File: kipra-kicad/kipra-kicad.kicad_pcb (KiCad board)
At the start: 2 copper layers, 128.2 x 134.8 mm, 51 parts

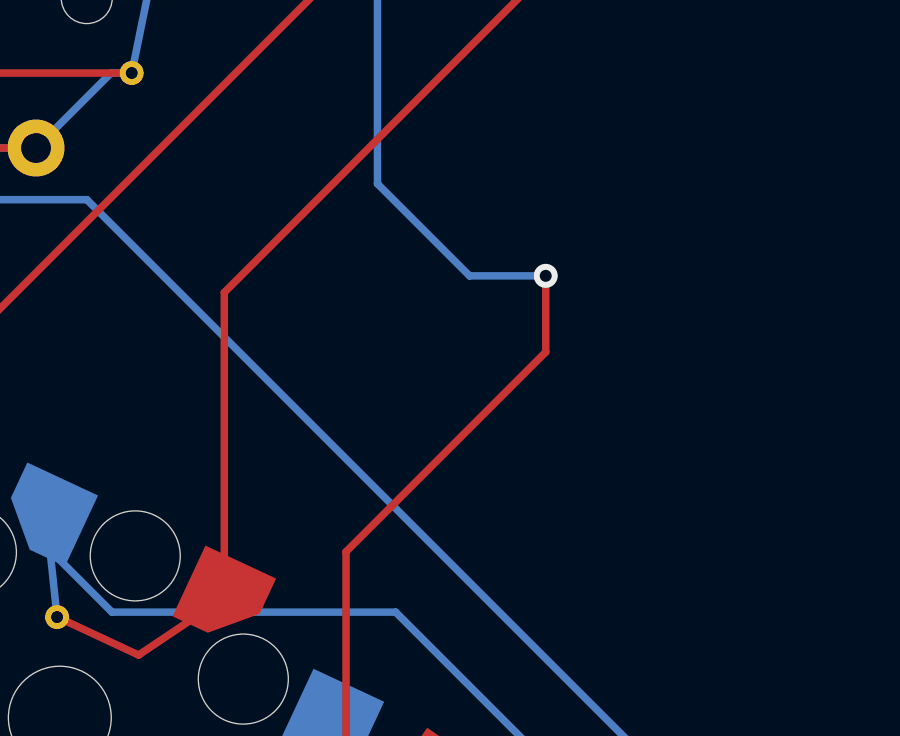
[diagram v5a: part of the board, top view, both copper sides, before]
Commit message: about to edit kicad pcb file by hand to fix row to mcu traces
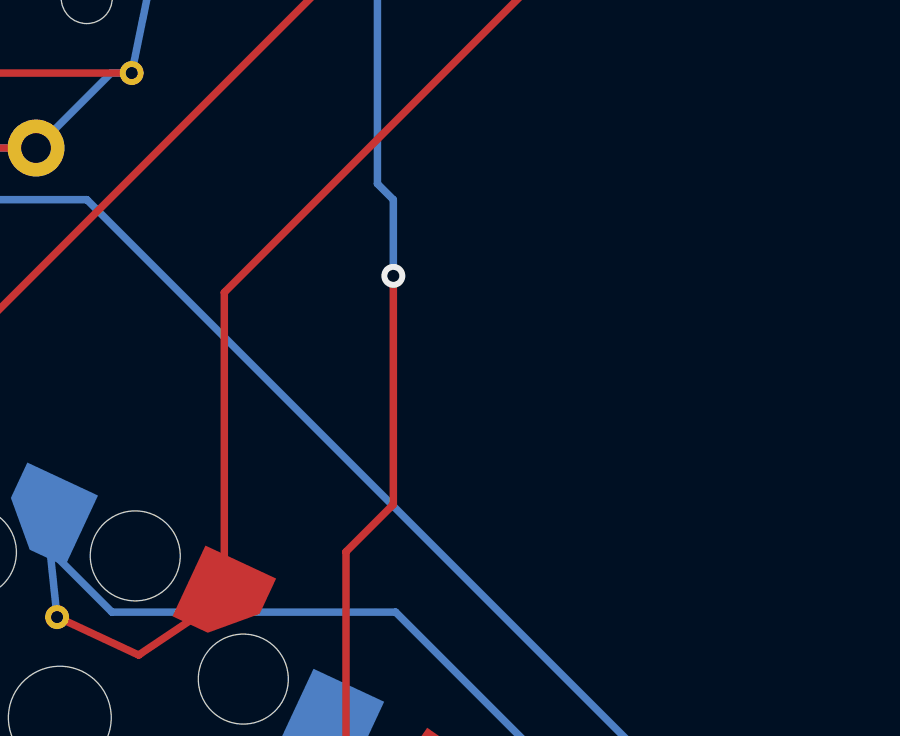
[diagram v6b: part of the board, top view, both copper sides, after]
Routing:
- net P07: track 158.1 -> 152.4 mm
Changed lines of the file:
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@@
   (segment (start 189.862146 123.877924) (end 162.504222 96.52) (width 0.25) (layer "B.Cu") (net 29))
   (segment (start 115.19 94.8) (end 117.35 94.8) (width 0.25) (layer "B.Cu") (net 29))
-  (segment (start 177.8 101.6) (end 171.142994 108.257006) (width 0.25) (layer "F.Cu") (net 30))
+  (segment (start 171.142994 123.996442) (end 172.808353 125.661801) (width 0.25) (layer "F.Cu") (net 30))
   (segment (start 172.19 80.35) (end 174.35 80.35) (width 0.25) (layer "F.Cu") (net 30))
+  (segment (start 172.72 106.68) (end 171.142994 108.257006) (width 0.25) (layer "F.Cu") (net 30))
   (segment (start 171.26 81.28) (end 172.19 80.35) (width 0.25) (layer "F.Cu") (net 30))
   (segment (start 115.19 77.8) (end 115.19 78.335305) (width 0.25) (layer "F.Cu") (net 30))
   (segment (start 98.35 88) (end 96.19 88) (width 0.25) (layer "F.Cu") (net 30))
+  (segment (start 172.72 99.06) (end 172.72 106.68) (width 0.25) (layer "F.Cu") (net 30))
   (segment (start 138.365 77.725) (end 153.115 77.725) (width 0.25) (layer "F.Cu") (net 30))
   (segment (start 119.125 76.025) (end 131.715 76.025) (width 0.25) (layer "F.Cu") (net 30))
   (segment (start 172.808353 125.661801) (end 173.338796 125.661801) (width 0.25) (layer "F.Cu") (net 30))
-  (segment (start 171.142994 123.996442) (end 172.808353 125.661801) (width 0.25) (layer "F.Cu") (net 30))
   (segment (start 158.83 81.28) (end 171.26 81.28) (width 0.25) (layer "F.Cu") (net 30))
   (segment (start 155.35 77.8) (end 158.83 81.28) (width 0.25) (layer "F.Cu") (net 30))
-  (segment (start 171.142994 108.257006) (end 171.142994 123.996442) (width 0.25) (layer "F.Cu") (net 30))
   (segment (start 131.715 76.025) (end 134.19 73.55) (width 0.25) (layer "F.Cu") (net 30))
   (segment (start 107.165305 86.36) (end 99.99 86.36) (width 0.25) (layer "F.Cu") (net 30))
   (segment (start 134.19 73.55) (end 138.365 77.725) (width 0.25) (layer "F.Cu") (net 30))
   (segment (start 99.99 86.36) (end 98.35 88) (width 0.25) (layer "F.Cu") (net 30))
+  (segment (start 171.142994 108.257006) (end 171.142994 123.996442) (width 0.25) (layer "F.Cu") (net 30))
   (segment (start 115.19 78.335305) (end 107.165305 86.36) (width 0.25) (layer "F.Cu") (net 30))
   (segment (start 117.35 77.8) (end 115.19 77.8) (width 0.25) (layer "F.Cu") (net 30))
@@
   (segment (start 153.19 77.8) (end 155.35 77.8) (width 0.25) (layer "F.Cu") (net 30))
   (segment (start 153.115 77.725) (end 153.19 77.8) (width 0.25) (layer "F.Cu") (net 30))
-  (segment (start 177.8 99.06) (end 177.8 101.6) (width 0.25) (layer "F.Cu") (net 30))
-  (via (at 177.8 99.06) (size 0.8) (drill 0.4) (layers "F.Cu" "B.Cu") (net 30))
+  (via (at 172.72 99.06) (size 0.8) (drill 0.4) (layers "F.Cu" "B.Cu") (net 30))
+  (segment (start 172.72 96.52) (end 172.19 95.99) (width 0.25) (layer "B.Cu") (net 30))
   (segment (start 172.808353 125.661801) (end 173.338796 125.661801) (width 0.25) (layer "B.Cu") (net 30))
-  (segment (start 177.8 99.06) (end 175.26 99.06) (width 0.25) (layer "B.Cu") (net 30))
+  (segment (start 172.72 99.06) (end 172.72 96.52) (width 0.25) (layer "B.Cu") (net 30))
   (segment (start 172.19 80.35) (end 174.35 80.35) (width 0.25) (layer "B.Cu") (net 30))
   (segment (start 153.19 77.8) (end 155.35 77.8) (width 0.25) (layer "B.Cu") (net 30))
   (segment (start 173.338796 125.661801) (end 174.577721 126.900726) (width 0.25) (layer "B.Cu") (net 30))
+  (segment (start 172.19 95.99) (end 172.19 80.35) (width 0.25) (layer "B.Cu") (net 30))
   (segment (start 134.19 73.55) (end 136.35 73.55) (width 0.25) (layer "B.Cu") (net 30))
   (segment (start 115.19 77.8) (end 117.35 77.8) (width 0.25) (layer "B.Cu") (net 30))
-  (segment (start 172.19 95.99) (end 172.19 80.35) (width 0.25) (layer "B.Cu") (net 30))
-  (segment (start 175.26 99.06) (end 172.19 95.99) (width 0.25) (layer "B.Cu") (net 30))
   (segment (start 98.35 88) (end 96.19 88) (width 0.25) (layer "B.Cu") (net 30))
   (segment (start 107.3 69.225) (end 115.19 61.335) (width 0.25) (layer "F.Cu") (net 31))

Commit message: hand editing pcb file seems to have fixed the row to mcu traces
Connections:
- D1 pad 1: P08 -> P8
- D10 pad 1: P07 -> P7
- D11 pad 1: P06 -> P6
- D12 pad 1: P05 -> P5
- D13 pad 1: P08 -> P8
- D14 pad 1: P07 -> P7
- D15 pad 1: P06 -> P6
- D16 pad 1: P05 -> P5
- D17 pad 1: P07 -> P7
- D18 pad 1: P06 -> P6
- D19 pad 1: P05 -> P5
- D2 pad 1: P07 -> P7
- D20 pad 1: P08 -> P8
- D21 pad 1: P07 -> P7
- D22 pad 1: P06 -> P6
- D3 pad 1: P06 -> P6
- D4 pad 1: P05 -> P5
- D5 pad 1: P08 -> P8
- D6 pad 1: P07 -> P7
- D7 pad 1: P06 -> P6
- D8 pad 1: P05 -> P5
- D9 pad 1: P08 -> P8
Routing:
- net P6: track 10.2 -> 183.6 mm
- net P06: track 173.4 -> 0.00 mm
- net P7: track 10.2 -> 162.6 mm, vias 0 -> 1
- net P07: track 152.4 -> 0.00 mm, vias 1 -> 0
- net P8: track 10.2 -> 151.7 mm
- net P08: track 141.6 -> 0.00 mm
- net P05: track 98.1 -> 0.00 mm
- net P5: track 10.2 -> 108.2 mm

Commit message: DRC passes!
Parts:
- MCU1: footprint nice_nano -> ceoloide:nice_nano
- moved _3 15.5 mm to (201.1, 84.8)
- moved D16 2.71 mm to (156.1, 41.2)
- moved MCU1 2.71 mm to (197.1, 43.8)
- moved D11 2.71 mm to (137.1, 54.0)
- moved D15 2.71 mm to (156.1, 58.2)
- moved D2 2.71 mm to (99.1, 85.4)
- moved S17 2.71 mm to (175.1, 72.8)
- moved S6 2.71 mm to (118.1, 70.2)
- moved S3 2.71 mm to (99.1, 63.4)
- moved S4 2.71 mm to (99.1, 46.4)
- moved D7 2.71 mm to (118.1, 58.2)
- moved S16 2.71 mm to (156.1, 36.2)
- moved _1 2.71 mm to (99.1, 110.2)
- moved S12 2.71 mm to (137.1, 32.0)
- moved _2 2.71 mm to (99.1, 33.7)
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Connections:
- MCU1 pad 13: MCU1_13 -> MCU1_12
- MCU1 pad 14: MCU1_14 -> MCU1_11
- MCU1 pad 15: MCU1_15 -> MCU1_10
- MCU1 pad 16: MCU1_16 -> MCU1_9
- MCU1 pad 17: MCU1_17 -> MCU1_8
- MCU1 pad 18: MCU1_18 -> MCU1_7
- MCU1 pad 19: MCU1_19 -> MCU1_6
- MCU1 pad 20: MCU1_20 -> MCU1_5
- MCU1 pad 21: MCU1_21 -> MCU1_4
- MCU1 pad 22: MCU1_22 -> MCU1_3
- MCU1 pad 23: MCU1_23 -> MCU1_2
- MCU1 pad 24: MCU1_24 -> MCU1_1
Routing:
- net P8: track 151.7 -> 246.3 mm
- net GND: track 96.4 -> 46.4 mm, vias 0 -> 2
- net P7: track 162.6 -> 211.3 mm, vias 1 -> 0
- net P6: track 183.6 -> 221.6 mm, vias 0 -> 1
- net P5: track 108.2 -> 138.3 mm
- net P19: track 185.2 -> 158.5 mm, vias 1 -> 0
- net P14: track 193.4 -> 166.8 mm
- net P10: track 258.3 -> 234.9 mm, vias 0 -> 1
- net VCC: track 87.8 -> 67.0 mm
- net P16: track 214.4 -> 194.2 mm
- net P15: track 167.4 -> 152.2 mm
- net P2: track 57.8 -> 53.5 mm
- net RAW: track 11.7 -> 9.63 mm
- net pinky_one: track 33.8 -> 35.3 mm
- net pinky_four: track 34.2 -> 35.3 mm
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- added copper zone on B.Cu, net GND
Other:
- outline, holes or cut-outs redrawn
